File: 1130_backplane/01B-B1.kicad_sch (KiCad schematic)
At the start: 86 parts

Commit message: DN101-DN111 added to backplane schematics, DN111 01B-A1 connections made, 01B-B1 connections to be made when all signals on connectors
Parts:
- removed J345, J346, J347, J348, J349, J350, J351, J352, J353, J354, J355, J356, J357, J358, J359, J360, J361, J362, J363, J364, J365, J366, J367, J368, J369, J370, J371, J372, J373, J374, J375, J376, J377, J378, J379, J380, J381, J382, J383, J384, J385, J386, J387, J388, J389, J390, J391, J392, J393, J394, J395, J396, J397, J398, J399, J400, J401, J402, J403, J404, J405, J406, J407, J408, J409, J410, J411, J412, J413, J414, J415, J416, J417, J418, J419, J420, J421, J422, J423, J424, J425, J426, J427, J428, J429, J430: ~, symbol Connector_Generic:Conn_02x12_Row_Letter_First
- added J? (x86): ~, symbol Connector_Generic:Conn_02x12_Row_Letter_First
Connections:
- net +3V: now also J?.b2 (Pin_b2), J?.b2 (Pin_b2), J?.b2 (Pin_b2), J?.b2 (Pin_b2), J?.b2 (Pin_b2), J?.b2 (Pin_b2), J?.b2 (Pin_b2), J?.b2 (Pin_b2), J?.b2 (Pin_b2), J?.b2 (Pin_b2), J?.b2 (Pin_b2), J?.b2 (Pin_b2), J?.b2 (Pin_b2), J?.b2 (Pin_b2), J?.b2 (Pin_b2), J?.b2 (Pin_b2), J?.b2 (Pin_b2), J?.b2 (Pin_b2), J?.b2 (Pin_b2), J?.b2 (Pin_b2), J?.b2 (Pin_b2), J?.b2 (Pin_b2), J?.b2 (Pin_b2), J?.b2 (Pin_b2), J?.b2 (Pin_b2), J?.b2 (Pin_b2), J?.b2 (Pin_b2), J?.b2 (Pin_b2), J?.b2 (Pin_b2), J?.b2 (Pin_b2), J?.b2 (Pin_b2), J?.b2 (Pin_b2), J?.b2 (Pin_b2), J?.b2 (Pin_b2), J?.b2 (Pin_b2), J?.b2 (Pin_b2), J?.b2 (Pin_b2), J?.b2 (Pin_b2), J?.b2 (Pin_b2), J?.b2 (Pin_b2), J?.b2 (Pin_b2), J?.b2 (Pin_b2), J?.b2 (Pin_b2), J?.b2 (Pin_b2), J?.b2 (Pin_b2), J?.b2 (Pin_b2), J?.b2 (Pin_b2), J?.b2 (Pin_b2), J?.b2 (Pin_b2), J?.b2 (Pin_b2), J?.b2 (Pin_b2), J?.b2 (Pin_b2), J?.b2 (Pin_b2), J?.b2 (Pin_b2), J?.b2 (Pin_b2), J?.b2 (Pin_b2), J?.b2 (Pin_b2), J?.b2 (Pin_b2), J?.b2 (Pin_b2), J?.b2 (Pin_b2), J?.b2 (Pin_b2), J?.b2 (Pin_b2), J?.b2 (Pin_b2), J?.b2 (Pin_b2), J?.b2 (Pin_b2), J?.b2 (Pin_b2), J?.b2 (Pin_b2), J?.b2 (Pin_b2), J?.b2 (Pin_b2), J?.b2 (Pin_b2), J?.b2 (Pin_b2), J?.b2 (Pin_b2), J?.b2 (Pin_b2), J?.b2 (Pin_b2), J?.b2 (Pin_b2), J?.b2 (Pin_b2), J?.b2 (Pin_b2), J?.b2 (Pin_b2)
- net +6V: now also J?.a10 (Pin_a10), J?.a10 (Pin_a10), J?.a10 (Pin_a10), J?.a10 (Pin_a10), J?.a10 (Pin_a10), J?.a10 (Pin_a10), J?.a10 (Pin_a10), J?.a10 (Pin_a10), J?.a10 (Pin_a10), J?.a10 (Pin_a10), J?.a10 (Pin_a10), J?.a10 (Pin_a10), J?.a10 (Pin_a10), J?.a10 (Pin_a10), J?.a10 (Pin_a10), J?.a10 (Pin_a10), J?.a10 (Pin_a10), J?.a10 (Pin_a10), J?.a10 (Pin_a10), J?.a10 (Pin_a10), J?.a10 (Pin_a10), J?.a10 (Pin_a10), J?.a10 (Pin_a10), J?.a10 (Pin_a10), J?.a10 (Pin_a10), J?.a10 (Pin_a10), J?.a10 (Pin_a10), J?.a10 (Pin_a10), J?.a10 (Pin_a10), J?.a10 (Pin_a10), J?.a10 (Pin_a10), J?.a10 (Pin_a10), J?.a10 (Pin_a10), J?.a10 (Pin_a10), J?.a10 (Pin_a10), J?.a10 (Pin_a10), J?.a10 (Pin_a10), J?.a10 (Pin_a10), J?.a10 (Pin_a10), J?.a10 (Pin_a10), J?.a10 (Pin_a10), J?.a10 (Pin_a10), J?.a10 (Pin_a10), J?.a10 (Pin_a10), J?.a10 (Pin_a10), J?.a10 (Pin_a10), J?.a10 (Pin_a10), J?.a10 (Pin_a10), J?.a10 (Pin_a10), J?.a10 (Pin_a10), J?.a10 (Pin_a10), J?.a10 (Pin_a10), J?.a10 (Pin_a10), J?.a10 (Pin_a10), J?.a10 (Pin_a10), J?.a10 (Pin_a10), J?.a10 (Pin_a10), J?.a10 (Pin_a10), J?.a10 (Pin_a10), J?.a10 (Pin_a10), J?.a10 (Pin_a10), J?.a10 (Pin_a10), J?.a10 (Pin_a10), J?.a10 (Pin_a10), J?.a10 (Pin_a10), J?.a10 (Pin_a10), J?.a10 (Pin_a10), J?.a10 (Pin_a10), J?.a10 (Pin_a10), J?.a10 (Pin_a10), J?.a10 (Pin_a10), J?.a10 (Pin_a10), J?.a10 (Pin_a10), J?.a10 (Pin_a10), J?.a10 (Pin_a10), J?.a10 (Pin_a10), J?.a10 (Pin_a10), J?.a10 (Pin_a10)
- net -3V: now also J?.a5 (Pin_a5), J?.a5 (Pin_a5), J?.a5 (Pin_a5), J?.a5 (Pin_a5), J?.a5 (Pin_a5), J?.a5 (Pin_a5), J?.a5 (Pin_a5), J?.a5 (Pin_a5), J?.a5 (Pin_a5), J?.a5 (Pin_a5), J?.a5 (Pin_a5), J?.a5 (Pin_a5), J?.a5 (Pin_a5), J?.a5 (Pin_a5), J?.a5 (Pin_a5), J?.a5 (Pin_a5), J?.a5 (Pin_a5), J?.a5 (Pin_a5), J?.a5 (Pin_a5), J?.a5 (Pin_a5), J?.a5 (Pin_a5), J?.a5 (Pin_a5), J?.a5 (Pin_a5), J?.a5 (Pin_a5), J?.a5 (Pin_a5), J?.a5 (Pin_a5), J?.a5 (Pin_a5), J?.a5 (Pin_a5), J?.a5 (Pin_a5), J?.a5 (Pin_a5), J?.a5 (Pin_a5), J?.a5 (Pin_a5), J?.a5 (Pin_a5), J?.a5 (Pin_a5), J?.a5 (Pin_a5), J?.a5 (Pin_a5), J?.a5 (Pin_a5), J?.a5 (Pin_a5), J?.a5 (Pin_a5), J?.a5 (Pin_a5), J?.a5 (Pin_a5), J?.a5 (Pin_a5), J?.a5 (Pin_a5), J?.a5 (Pin_a5), J?.a5 (Pin_a5), J?.a5 (Pin_a5), J?.a5 (Pin_a5), J?.a5 (Pin_a5), J?.a5 (Pin_a5), J?.a5 (Pin_a5), J?.a5 (Pin_a5), J?.a5 (Pin_a5), J?.a5 (Pin_a5), J?.a5 (Pin_a5), J?.a5 (Pin_a5), J?.a5 (Pin_a5), J?.a5 (Pin_a5), J?.a5 (Pin_a5), J?.a5 (Pin_a5), J?.a5 (Pin_a5), J?.a5 (Pin_a5), J?.a5 (Pin_a5), J?.a5 (Pin_a5), J?.a5 (Pin_a5), J?.a5 (Pin_a5), J?.a5 (Pin_a5), J?.a5 (Pin_a5), J?.a5 (Pin_a5), J?.a5 (Pin_a5), J?.a5 (Pin_a5), J?.a5 (Pin_a5), J?.a5 (Pin_a5), J?.a5 (Pin_a5), J?.a5 (Pin_a5), J?.a5 (Pin_a5), J?.a5 (Pin_a5), J?.a5 (Pin_a5), J?.a5 (Pin_a5)
- net -IO_BIT_0: now also J?.a1 (Pin_a1), J?.a1 (Pin_a1)
- net -IO_BIT_1: now also J?.b1 (Pin_b1), J?.b1 (Pin_b1)
- net -IO_BIT_10: now also J?.a7 (Pin_a7), J?.a7 (Pin_a7)
- net -IO_BIT_11: now also J?.b8 (Pin_b8), J?.b8 (Pin_b8)
- net -IO_BIT_12: now also J?.a8 (Pin_a8), J?.a8 (Pin_a8)
- net -IO_BIT_13: now also J?.b9 (Pin_b9), J?.b9 (Pin_b9)
- net -IO_BIT_14: now also J?.a9 (Pin_a9), J?.a9 (Pin_a9)
- net -IO_BIT_15: now also J?.b10 (Pin_b10), J?.b10 (Pin_b10)
- net -IO_BIT_2: now also J?.a2 (Pin_a2), J?.a2 (Pin_a2)
- net -IO_BIT_3: now also J?.b3 (Pin_b3), J?.b3 (Pin_b3)
- net -IO_BIT_4: now also J?.a3 (Pin_a3), J?.a3 (Pin_a3)
- net -IO_BIT_5: now also J?.b4 (Pin_b4), J?.b4 (Pin_b4)
- net -IO_BIT_6: now also J?.a4 (Pin_a4), J?.a4 (Pin_a4)
- net -IO_BIT_7: now also J?.b5 (Pin_b5), J?.b5 (Pin_b5)
- net -IO_BIT_8: now also J?.a6 (Pin_a6), J?.a6 (Pin_a6)
- net -IO_BIT_9: now also J?.b6 (Pin_b6), J?.b6 (Pin_b6)
- net GND: now also J?.b7 (Pin_b7), J?.b7 (Pin_b7), J?.b7 (Pin_b7), J?.b7 (Pin_b7), J?.b7 (Pin_b7), J?.b7 (Pin_b7), J?.b7 (Pin_b7), J?.b7 (Pin_b7), J?.b7 (Pin_b7), J?.b7 (Pin_b7), J?.b7 (Pin_b7), J?.b7 (Pin_b7), J?.b7 (Pin_b7), J?.b7 (Pin_b7), J?.b7 (Pin_b7), J?.b7 (Pin_b7), J?.b7 (Pin_b7), J?.b7 (Pin_b7), J?.b7 (Pin_b7), J?.b7 (Pin_b7), J?.b7 (Pin_b7), J?.b7 (Pin_b7), J?.b7 (Pin_b7), J?.b7 (Pin_b7), J?.b7 (Pin_b7), J?.b7 (Pin_b7), J?.b7 (Pin_b7), J?.b7 (Pin_b7), J?.b7 (Pin_b7), J?.b7 (Pin_b7), J?.b7 (Pin_b7), J?.b7 (Pin_b7), J?.b7 (Pin_b7), J?.b7 (Pin_b7), J?.b7 (Pin_b7), J?.b7 (Pin_b7), J?.b7 (Pin_b7), J?.b7 (Pin_b7), J?.b7 (Pin_b7), J?.b7 (Pin_b7), J?.b7 (Pin_b7), J?.b7 (Pin_b7), J?.b7 (Pin_b7), J?.b7 (Pin_b7), J?.b7 (Pin_b7), J?.b7 (Pin_b7), J?.b7 (Pin_b7), J?.b7 (Pin_b7), J?.b7 (Pin_b7), J?.b7 (Pin_b7), J?.b7 (Pin_b7), J?.b7 (Pin_b7), J?.b7 (Pin_b7), J?.b7 (Pin_b7), J?.b7 (Pin_b7), J?.b7 (Pin_b7), J?.b7 (Pin_b7), J?.b7 (Pin_b7), J?.b7 (Pin_b7), J?.b7 (Pin_b7), J?.b7 (Pin_b7), J?.b7 (Pin_b7), J?.b7 (Pin_b7), J?.b7 (Pin_b7), J?.b7 (Pin_b7), J?.b7 (Pin_b7), J?.b7 (Pin_b7), J?.b7 (Pin_b7), J?.b7 (Pin_b7), J?.b7 (Pin_b7), J?.b7 (Pin_b7), J?.b7 (Pin_b7), J?.b7 (Pin_b7), J?.b7 (Pin_b7), J?.b7 (Pin_b7), J?.b7 (Pin_b7), J?.b7 (Pin_b7), J?.b7 (Pin_b7), J?.b7 (Pin_b7), J?.b7 (Pin_b7), J?.b7 (Pin_b7), J?.b7 (Pin_b7), J?.b7 (Pin_b7), J?.b7 (Pin_b7), J?.b7 (Pin_b7), J?.b7 (Pin_b7)

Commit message: Add labels for cable runs, completed tracing for DN111 from previous commit, decided it would be too much work to go back and route later... Completed DN201 page.
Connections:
- net +3V: no longer J?.b2 (Pin_b2), J?.b2 (Pin_b2)
- net +6V: no longer J?.a10 (Pin_a10), J?.a10 (Pin_a10)
- net -3V: no longer J?.a5 (Pin_a5), J?.a5 (Pin_a5)
- net -ADD_SUB_OR_EOR_GATE: now reaches J?.a9 (Pin_a9)
- net -ADD_SUB_EOR_GATE: now reaches J?.b9 (Pin_b9)
- net -AND_SPD_GATE: now reaches J?.a3 (Pin_a3)
- net DN201_AL4: now reaches J?.b3 (Pin_b3)
- net -XIO_E2_R_W: now reaches J?.b4 (Pin_b4)
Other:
- note added: "5803291"
- note added: "CABL 01A-C1N2"
- note added: "CABL 01B-A1N7"
- note added: "CABL 01B-B1A3"
- note added: "CABL 01B-B1A4"

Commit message: Add labels for bottom T[x] connectors, finished page DU101.
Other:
- moved on the sheet: J?

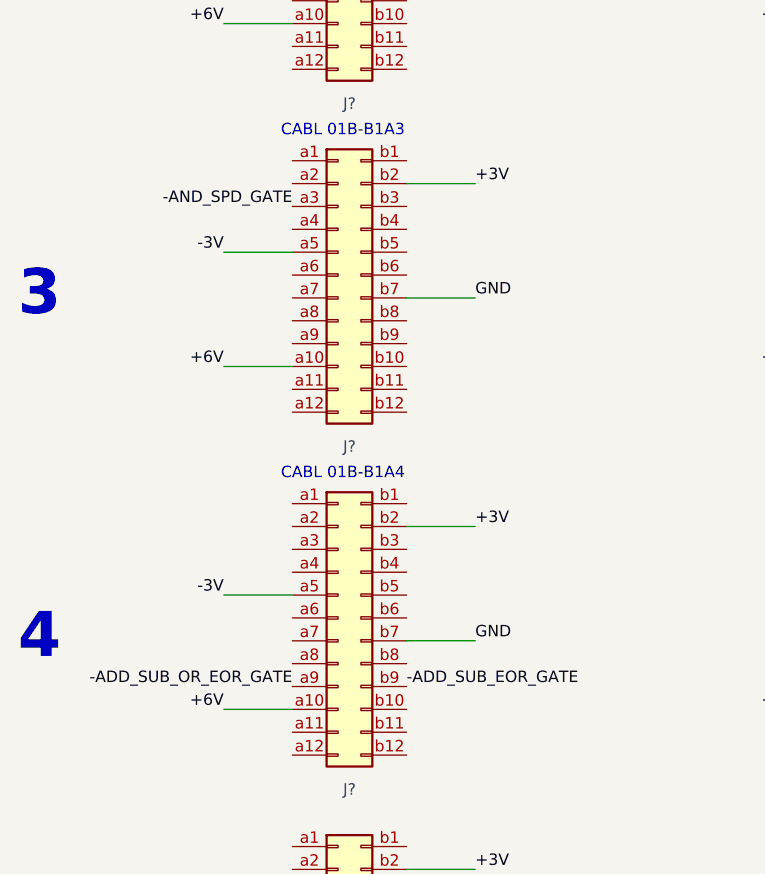
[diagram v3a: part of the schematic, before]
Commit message: Finish page KA101-KA111
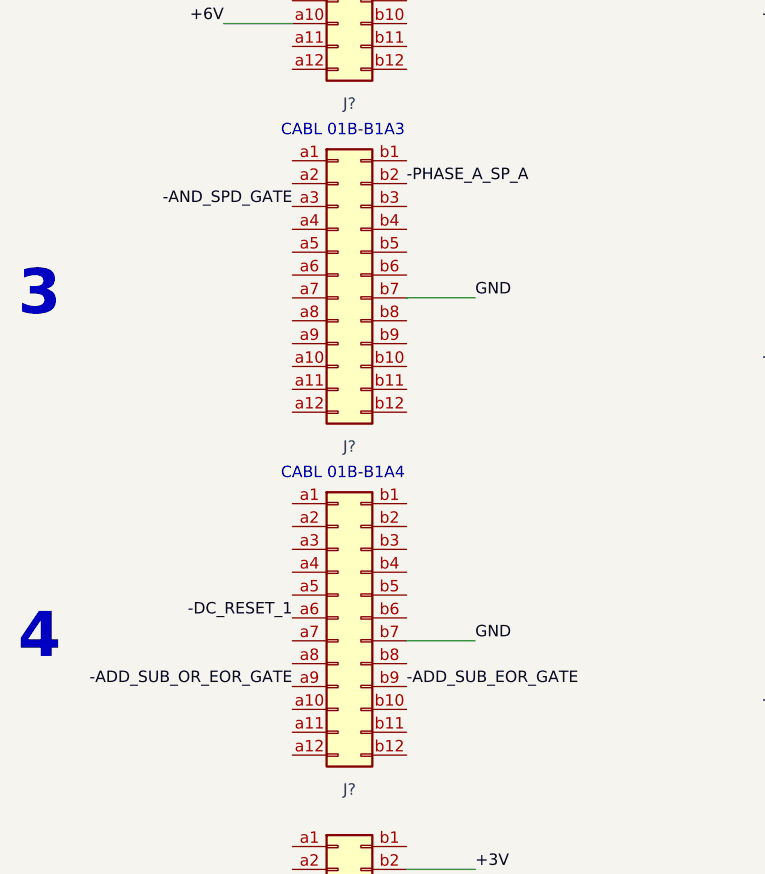
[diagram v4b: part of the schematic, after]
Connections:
- net +3V: no longer J?.b2 (Pin_b2), J?.b2 (Pin_b2)
- net +6V: no longer J?.a10 (Pin_a10), J?.a10 (Pin_a10)
- net -3V: no longer J?.a5 (Pin_a5), J?.a5 (Pin_a5)
- net -DC_RESET_1: now reaches J?.a6 (Pin_a6)
- new net -PHASE_A_SP_A: J?.b2 (Pin_b2)
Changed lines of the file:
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@@
-    (stroke (width 0) (type default) (color 0 0 0 0))
-  )
-  (wire (pts (xy 45.72 144.78) (xy 53.34 144.78))
     (stroke (width 0) (type default) (color 0 0 0 0))
   )
@@
     (stroke (width 0) (type default) (color 0 0 0 0))
   )
-  (wire (pts (xy 25.4 203.2) (xy 33.02 203.2))
-    (stroke (width 0) (type default) (color 0 0 0 0))
-  )
   (wire (pts (xy 152.4 190.5) (xy 160.02 190.5))
     (stroke (width 0) (type default) (color 0 0 0 0))
@@
     (stroke (width 0) (type solid) (color 0 0 0 0))
   )
-  (wire (pts (xy 25.4 165.1) (xy 33.02 165.1))
-    (stroke (width 0) (type default) (color 0 0 0 0))
-  )
   (wire (pts (xy 596.9 203.2) (xy 604.52 203.2))
     (stroke (width 0) (type default) (color 0 0 0 0))
@@
     (stroke (width 0) (type default) (color 0 0 0 0))
   )
-  (wire (pts (xy 25.4 152.4) (xy 33.02 152.4))
-    (stroke (width 0) (type default) (color 0 0 0 0))
-  )
   (polyline (pts (xy 34.29 49.53) (xy 35.56 49.53))
     (stroke (width 0) (type solid) (color 0 0 0 0))
@@
     (stroke (width 0) (type default) (color 0 0 0 0))
   )
-  (wire (pts (xy 25.4 190.5) (xy 33.02 190.5))
-    (stroke (width 0) (type default) (color 0 0 0 0))
-  )
   (wire (pts (xy 723.9 152.4) (xy 731.52 152.4))
     (stroke (width 0) (type default) (color 0 0 0 0))
@@
     (stroke (width 0) (type default) (color 0 0 0 0))
   )
-  (wire (pts (xy 45.72 182.88) (xy 53.34 182.88))
-    (stroke (width 0) (type default) (color 0 0 0 0))
-  )
   (wire (pts (xy 406.4 228.6) (xy 414.02 228.6))
     (stroke (width 0) (type default) (color 0 0 0 0))
@@
     (effects (font (size 1.27 1.27)) (justify left bottom))
   )
+  (label "-DC_RESET_1" (at 33.02 193.04 180)
+    (effects (font (size 1.27 1.27)) (justify right bottom))
+  )
   (label "+6V" (at 787.4 279.4 180)
     (effects (font (size 1.27 1.27)) (justify right bottom))
@@
     (effects (font (size 1.27 1.27)) (justify left bottom))
   )
-  (label "+3V" (at 53.34 144.78 0)
-    (effects (font (size 1.27 1.27)) (justify left bottom))
-  )
   (label "GND" (at 243.84 271.78 0)
     (effects (font (size 1.27 1.27)) (justify left bottom))
@@
     (effects (font (size 1.27 1.27)) (justify right bottom))
   )
-  (label "+6V" (at 25.4 203.2 180)
-    (effects (font (size 1.27 1.27)) (justify right bottom))
-  )
   (label "GND" (at 688.34 195.58 0)
     (effects (font (size 1.27 1.27)) (justify left bottom))
@@
     (effects (font (size 1.27 1.27)) (justify left bottom))
   )
-  (label "+3V" (at 53.34 182.88 0)
-    (effects (font (size 1.27 1.27)) (justify left bottom))
-  )
   (label "GND" (at 561.34 157.48 0)
     (effects (font (size 1.27 1.27)) (justify left bottom))
@@
     (effects (font (size 1.27 1.27)) (justify left bottom))
   )
-  (label "+6V" (at 25.4 165.1 180)
-    (effects (font (size 1.27 1.27)) (justify right bottom))
-  )
   (label "-3V" (at 787.4 152.4 180)
     (effects (font (size 1.27 1.27)) (justify right bottom))
@@
     (effects (font (size 1.27 1.27)) (justify left bottom))
   )
+  (label "-PHASE_A_SP_A" (at 45.72 144.78 0)
+    (effects (font (size 1.27 1.27)) (justify left bottom))
+  )
   (label "-IO_BIT_11" (at 744.22 236.22 0)
     (effects (font (size 1.27 1.27)) (justify left bottom))
@@
     (effects (font (size 1.27 1.27)) (justify right bottom))
   )
-  (label "-3V" (at 25.4 152.4 180)
-    (effects (font (size 1.27 1.27)) (justify right bottom))
-  )
   (label "-IO_BIT_9" (at 852.17 224.79 0)
     (effects (font (size 1.27 1.27)) (justify left bottom))
@@
     (effects (font (size 1.27 1.27)) (justify left bottom))
   )
-  (label "-3V" (at 25.4 190.5 180)
-    (effects (font (size 1.27 1.27)) (justify right bottom))
-  )
   (label "GND" (at 751.84 157.48 0)

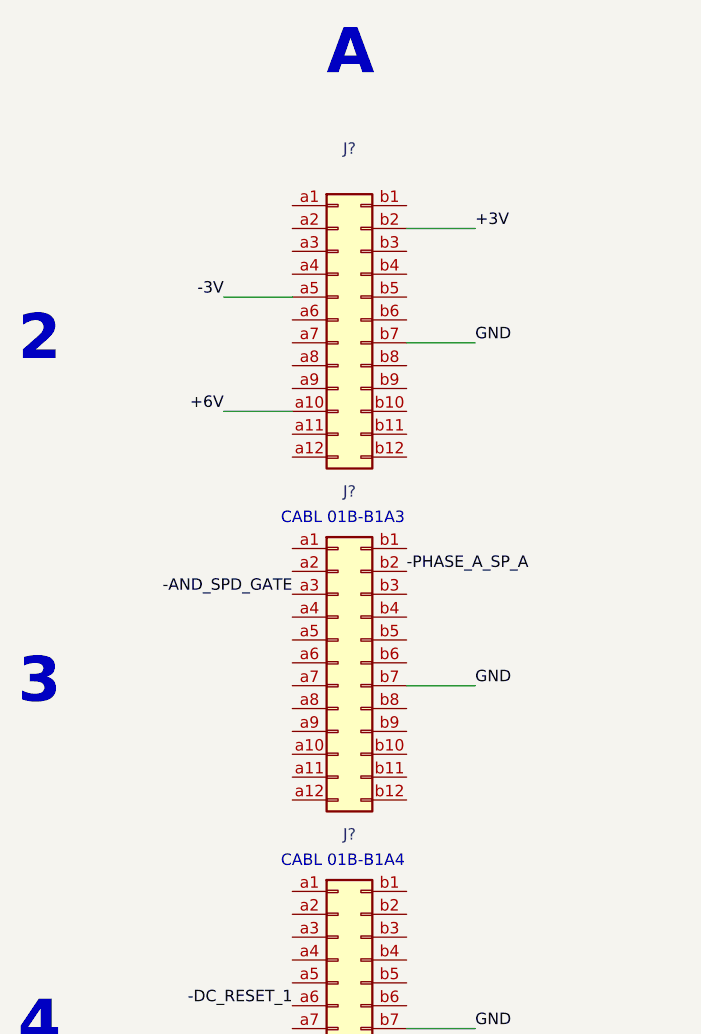
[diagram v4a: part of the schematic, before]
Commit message: Finish page KB101-KB111
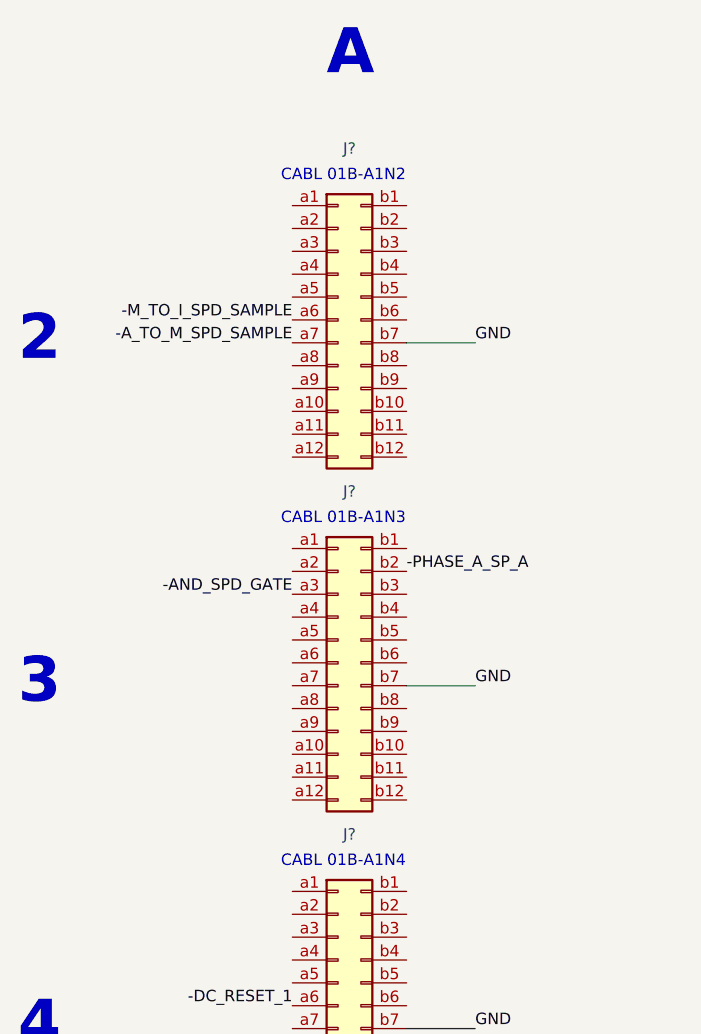
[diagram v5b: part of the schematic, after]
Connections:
- net +3V: no longer J?.b2 (Pin_b2)
- net +6V: no longer J?.a10 (Pin_a10)
- net -3V: no longer J?.a5 (Pin_a5)
- net -M_TO_I_SPD_SAMPLE: now reaches J?.a6 (Pin_a6)
- net -A_TO_M_SPD_SAMPLE: now reaches J?.a7 (Pin_a7)
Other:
- note added: "CABL 01B-A1N2"
- note added: "CABL 01B-A1N3"
- note added: "CABL 01B-A1N4"
- note removed: "CABL 01B-B1A3"
- note removed: "CABL 01B-B1A4"
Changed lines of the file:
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@@
     (stroke (width 0) (type solid) (color 0 0 0 0))
-  )
-  (wire (pts (xy 25.4 127) (xy 33.02 127))
-    (stroke (width 0) (type default) (color 0 0 0 0))
   )
   (polyline (pts (xy 307.34 27.94) (xy 308.61 27.94))
@@
     (stroke (width 0) (type solid) (color 0 0 0 0))
   )
-  (wire (pts (xy 25.4 114.3) (xy 33.02 114.3))
-    (stroke (width 0) (type default) (color 0 0 0 0))
-  )
   (wire (pts (xy 279.4 228.6) (xy 287.02 228.6))
     (stroke (width 0) (type default) (color 0 0 0 0))
@@
     (stroke (width 0) (type solid) (color 0 0 0 0))
   )
-  (wire (pts (xy 45.72 106.68) (xy 53.34 106.68))
-    (stroke (width 0) (type default) (color 0 0 0 0))
-  )
   (wire (pts (xy 363.22 157.48) (xy 370.84 157.48))
     (stroke (width 0) (type default) (color 0 0 0 0))
@@
     (effects (font (size 1.27 1.27)) (justify left bottom))
   )
-  (text "CABL 01B-B1A4" (at 31.75 177.8 0)
+  (text "CABL 01B-A1N4" (at 31.75 177.8 0)
     (effects (font (size 1.27 1.27)) (justify left bottom))
   )
@@
     (effects (font (size 5 5) (thickness 1) bold) (justify left bottom))
   )
-  (text "CABL 01B-B1A3" (at 31.75 139.7 0)
+  (text "CABL 01B-A1N3" (at 31.75 139.7 0)
     (effects (font (size 1.27 1.27)) (justify left bottom))
   )
@@
     (effects (font (size 1.27 1.27)) (justify left bottom))
   )
+  (text "CABL 01B-A1N2" (at 31.75 101.6 0)
+    (effects (font (size 1.27 1.27)) (justify left bottom))
+  )
   (text "T2" (at 397.51 33.02 0)
     (effects (font (size 5 5) (thickness 1) bold) (justify left bottom))
@@
     (effects (font (size 1.27 1.27)) (justify left bottom))
   )
-  (label "+6V" (at 25.4 127 180)
-    (effects (font (size 1.27 1.27)) (justify right bottom))
-  )
   (label "-3V" (at 723.9 228.6 180)
     (effects (font (size 1.27 1.27)) (justify right bottom))
@@
     (effects (font (size 1.27 1.27)) (justify right bottom))
   )
+  (label "-M_TO_I_SPD_SAMPLE" (at 33.02 116.84 180)
+    (effects (font (size 1.27 1.27)) (justify right bottom))
+  )
   (label "-IO_BIT_9" (at 852.17 224.79 0)
     (effects (font (size 1.27 1.27)) (justify left bottom))
@@
     (effects (font (size 1.27 1.27)) (justify left bottom))
   )
-  (label "-3V" (at 25.4 114.3 180)
-    (effects (font (size 1.27 1.27)) (justify right bottom))
-  )
   (label "-3V" (at 533.4 152.4 180)
     (effects (font (size 1.27 1.27)) (justify right bottom))
@@
     (effects (font (size 1.27 1.27)) (justify right bottom))
   )
-  (label "+3V" (at 53.34 106.68 0)
-    (effects (font (size 1.27 1.27)) (justify left bottom))
+  (label "-A_TO_M_SPD_SAMPLE" (at 33.02 119.38 180)
+    (effects (font (size 1.27 1.27)) (justify right bottom))
   )
   (label "+6V" (at 596.9 279.4 180)

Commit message: Finish page KD101-KD111
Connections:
- net +GT_B_BITS_0_TO_9_TO_OP_REG: now reaches J?.a9 (Pin_a9)
- net +I1_POWERED: now reaches J?.a2 (Pin_a2)
- net +I2_CYCLE: now reaches J?.a3 (Pin_a3)
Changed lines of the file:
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@@
+    (effects (font (size 1.27 1.27)) (justify right bottom))
+  )
+  (label "+I2_CYCLE" (at 33.02 299.72 180)
     (effects (font (size 1.27 1.27)) (justify right bottom))
   )
@@
     (effects (font (size 1.27 1.27)) (justify left bottom))
   )
+  (label "+I1_POWERED" (at 33.02 297.18 180)
+    (effects (font (size 1.27 1.27)) (justify right bottom))
+  )
   (label "GND" (at 497.84 271.78 0)
     (effects (font (size 1.27 1.27)) (justify left bottom))
@@
     (effects (font (size 1.27 1.27)) (justify right bottom))
   )
+  (label "+GT_B_BITS_0_TO_9_TO_OP_REG" (at 33.02 162.56 180)
+    (effects (font (size 1.27 1.27)) (justify right bottom))
+  )

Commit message: Redo annotations...
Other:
- note added: "5803757"
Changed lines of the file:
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@@
+    (effects (font (size 1.27 1.27)) (justify left bottom))
+  )
+  (text "5803757" (at 416.56 101.6 0)
     (effects (font (size 1.27 1.27)) (justify left bottom))
   )
@@
     (effects (font (size 5 5) (thickness 1) bold) (justify left bottom))
   )
+  (text "5803757" (at 353.06 101.6 0)
+    (effects (font (size 1.27 1.27)) (justify left bottom))
+  )
   (text "A" (at 331.47 368.3 0)

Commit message: Redo annotations...
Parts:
- gave numbers to parts that had none: 86
